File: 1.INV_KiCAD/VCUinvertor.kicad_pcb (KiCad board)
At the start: 2 copper layers, 100.7 x 138.5 mm, 153 parts, among them J14 FAN1, J15 FAN2, J16 PUMP1, J17 PUMP2, J7 PowerSupply, J9 BRAKE LIGHT, K1 IM06DGR, Q1 2N7002, Q10 2N7002, Q13 BC848C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

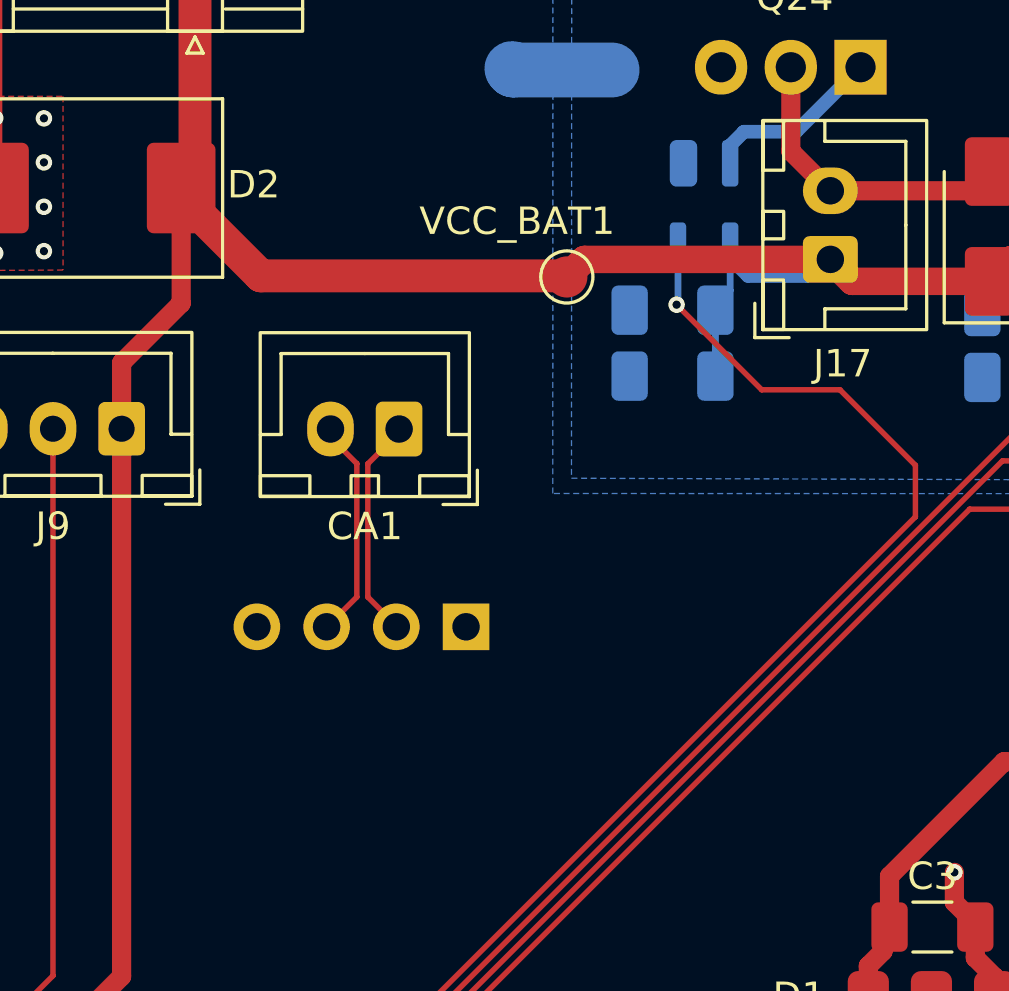
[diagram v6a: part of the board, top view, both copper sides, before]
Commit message: CAN_IN + CAN_OUT added
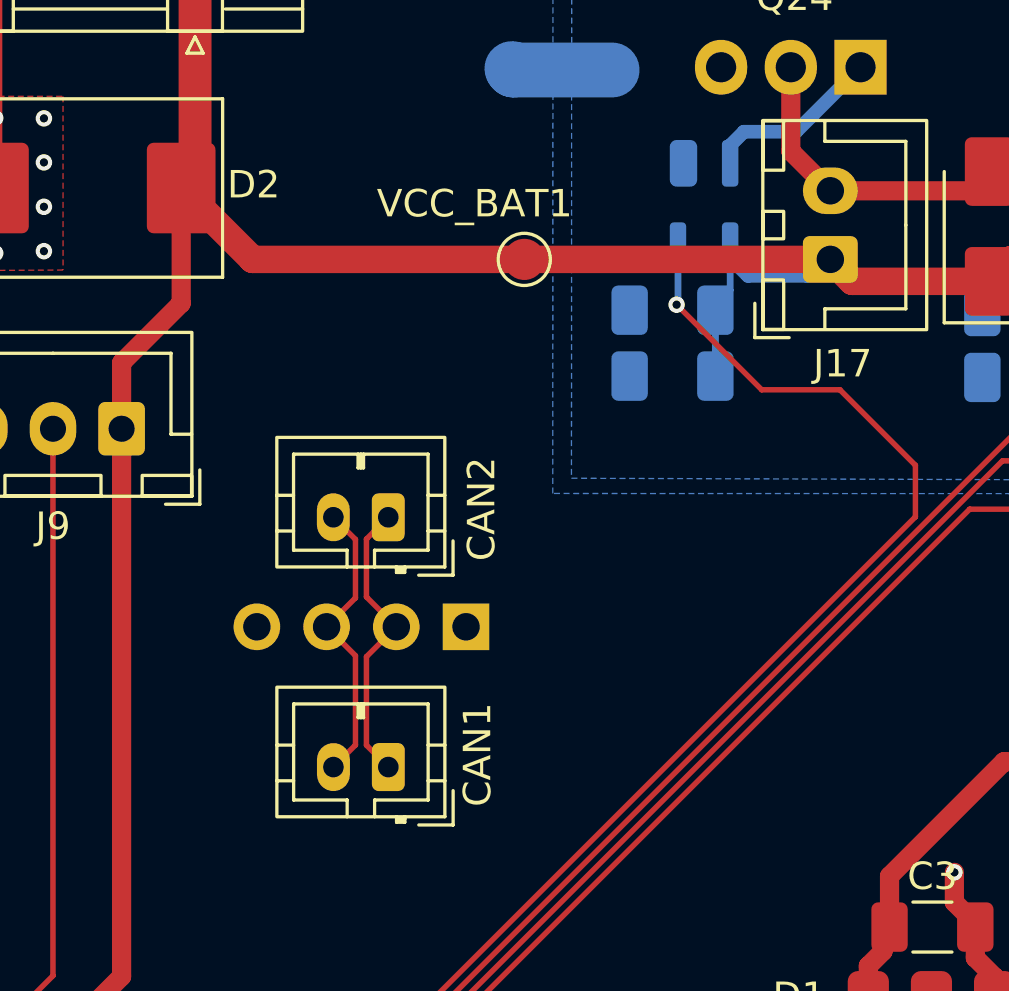
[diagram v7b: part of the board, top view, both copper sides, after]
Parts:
- added CAN2: CAN_OUT_NXP, Connector_JST:JST_PH_B2B-PH-K_1x02_P2.00mm_Vertical, F.Cu at (81.6, 57.4)
- CAN1: renamed from CA1; value CAN_OUT_NXP -> CAN_IN_NXP; footprint Connector_JST:JST_XH_B2B-XH-A_1x02_P2.50mm_Vertical -> Connector_JST:JST_PH_B2B-PH-K_1x02_P2.00mm_Vertical
- moved CAN1 12.3 mm to (81.6, 66.5)
- moved VCC_BAT1 1.68 mm to (86.6, 48.0)
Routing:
- net Net-(CA0-Pin_3): track 8.24 -> 10.6 mm
- net Net-(CA0-Pin_2): track 8.50 -> 10.7 mm

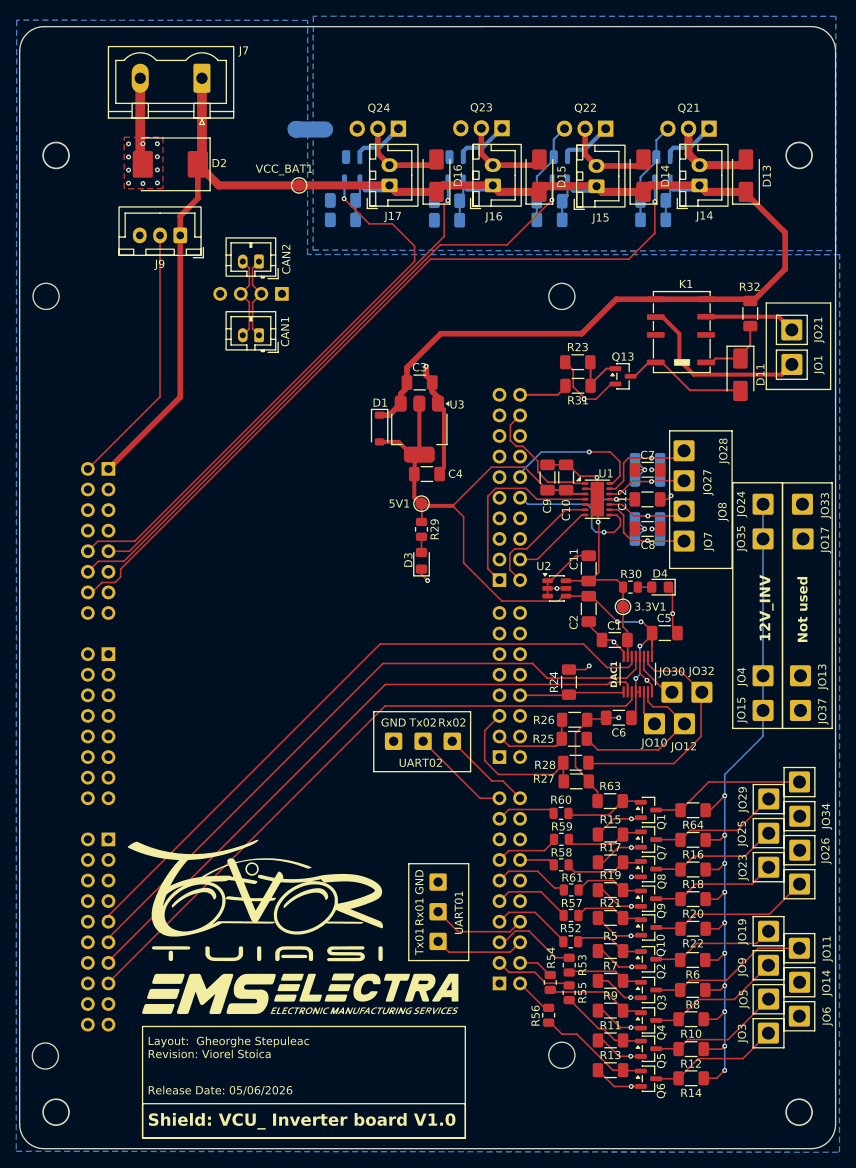
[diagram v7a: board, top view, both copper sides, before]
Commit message: CAN: TJA1448 Footprint correction
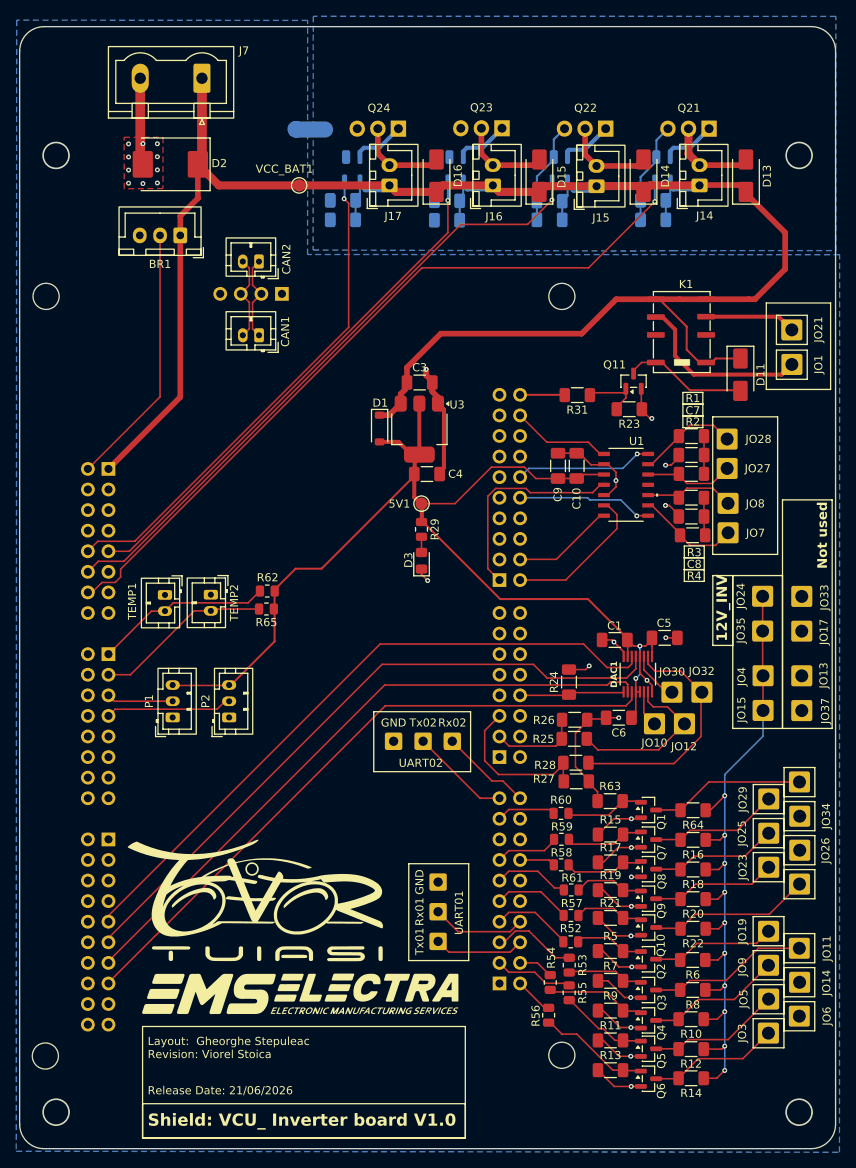
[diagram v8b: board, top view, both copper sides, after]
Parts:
- removed 3.3V1: 3.3V, TestPoint:TestPoint_Pad_D1.5mm
- removed C11: 10uF, Capacitor_SMD:C_1206_3216Metric_Pad1.33x1.80mm_HandSolder
- removed C12, C2: 0.1uF, Capacitor_SMD:C_1206_3216Metric_Pad1.33x1.80mm_HandSolder
- removed D4: LED, LED_SMD:LED_0805_2012Metric_Pad1.15x1.40mm_HandSolder
- removed Q13: BC848C, Package_TO_SOT_SMD:SOT-23
- removed R30: 1k, Resistor_SMD:R_0805_2012Metric
- removed R32: 360R, Resistor_SMD:R_1206_3216Metric_Pad1.30x1.75mm_HandSolder
- removed U2: REF3433T, Package_TO_SOT_SMD:SOT-23-6
- added P1: PRESSURE SENSOR 1, Connector_JST:JST_PH_B3B-PH-K_1x03_P2.00mm_Vertical, F.Cu at (70.9, 113.7)
- added P2: PRESSURE SENSOR 2, Connector_JST:JST_PH_B3B-PH-K_1x03_P2.00mm_Vertical, F.Cu at (77.9, 113.7)
- added Q11: 2N7002, Package_TO_SOT_SMD:SOT-23, F.Cu at (127.8, 72.2)
- added R62: 10k, Resistor_SMD:R_0805_2012Metric, F.Cu at (82.6, 98.1)
- added R65: 10k, Resistor_SMD:R_0805_2012Metric, F.Cu at (82.5, 100.3)
- added TEMP1: NTC1, Connector_JST:JST_PH_B2B-PH-K_1x02_P2.00mm_Vertical, F.Cu at (70.0, 98.6)
- added TEMP2: NTC2, Connector_JST:JST_PH_B2B-PH-K_1x02_P2.00mm_Vertical, F.Cu at (75.7, 98.6)
- R1, R2, R3, R4: moved to F.Cu
- R23: value 47k -> 100k
- R31: value 1k -> 100R
- U1: footprint Package_DFN_QFN:DFN-14-1EP_3x4.5mm_P0.65mm_EP1.65x4.25mm -> TJA1448:NXP-TJA1448A_NXP
- moved JO17 11.4 mm to (148.6, 103.1)
- moved JO33 11.4 mm to (148.6, 98.8)
- moved JO24 11.4 mm to (143.8, 98.8)
- moved JO35 11.4 mm to (143.8, 103.0)
- moved R23 8.60 mm to (127.3, 75.7), turned to 180 degrees
- moved R1 6.16 mm to (135.0, 79.0), turned to 0 degrees
- moved R3 6.04 mm to (135.0, 86.6), turned to 0 degrees
- moved C7 5.71 mm to (135.0, 81.3), turned to 0 degrees
- moved C8 5.62 mm to (135.0, 88.9), turned to 0 degrees
- moved R4 5.58 mm to (135.1, 91.2), turned to 180 degrees
- moved JO7 5.54 mm to (139.5, 90.9)
- moved JO27 5.53 mm to (139.4, 83.0)
- moved JO8 5.51 mm to (139.5, 87.3)
- moved JO28 5.51 mm to (139.4, 79.3)
- moved R2 5.45 mm to (135.0, 83.6), turned to 180 degrees
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- renumbered J9 to BR1
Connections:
- C1 pad 1: +3.3V -> +5V
- D11 pad 1: Net-(D11-K) -> BAT+
- DAC1 pad 7: +3.3V -> +5V
- K1 pad 1: Net-(D11-K) -> BAT+
- NXP11 pad 3: NXP_TPSOUT01 -> unconnected-(NXP11-Pin_3-Pad3)
- NXP11 pad 5: NXP_TPSOUT02 -> unconnected-(NXP11-Pin_5-Pad5)
- NXP14 pad 1: unconnected-(NXP14-Pin_1-Pad1) -> /TEMP1
- NXP14 pad 3: unconnected-(NXP14-Pin_3-Pad3) -> /TEMP2
- NXP14 pad 5: unconnected-(NXP14-Pin_5-Pad5) -> /PRES1
- NXP14 pad 7: unconnected-(NXP14-Pin_7-Pad7) -> /PRES2
- U1 pad 11: +3.3V -> unconnected-(U1-VIO-Pad11)
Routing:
- net +5V: track 96.3 -> 142.1 mm, vias 4 -> 2
- net +3.3V: track 32.0 -> 0.00 mm, vias 2 -> 0
- net GND: track 191.8 -> 167.3 mm, vias 33 -> 31
- net /TEMP2: track 0.00 -> 21.9 mm
- net /TEMP1: track 0.00 -> 21.9 mm
- net /PRES2: track 0.00 -> 15.6 mm
- net BAT+: track 234.6 -> 250.0 mm
- net /12V_INV: track 99.6 -> 88.4 mm
- net Net-(D11-K): track 9.17 -> 0.00 mm
- net /PUMP2: track 70.3 -> 61.9 mm
- net /PRES1: track 0.00 -> 8.23 mm
- net /TX1: track 15.8 -> 12.3 mm
- net /TX2: track 16.1 -> 19.1 mm
- net /RX1: track 23.9 -> 26.3 mm
- net /FAN1: track 95.3 -> 93.0 mm
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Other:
- board text added: "Meter (D-Gray)"
- board text added: "Release Date: 21/06/2026"
- board text removed: "Meter (D Gray)"
- board text removed: "Release Date: 05/06/2026"
